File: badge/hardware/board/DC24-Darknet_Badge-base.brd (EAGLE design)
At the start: 48.3 x 83.8 mm, 15 parts, among them U1 SOP22

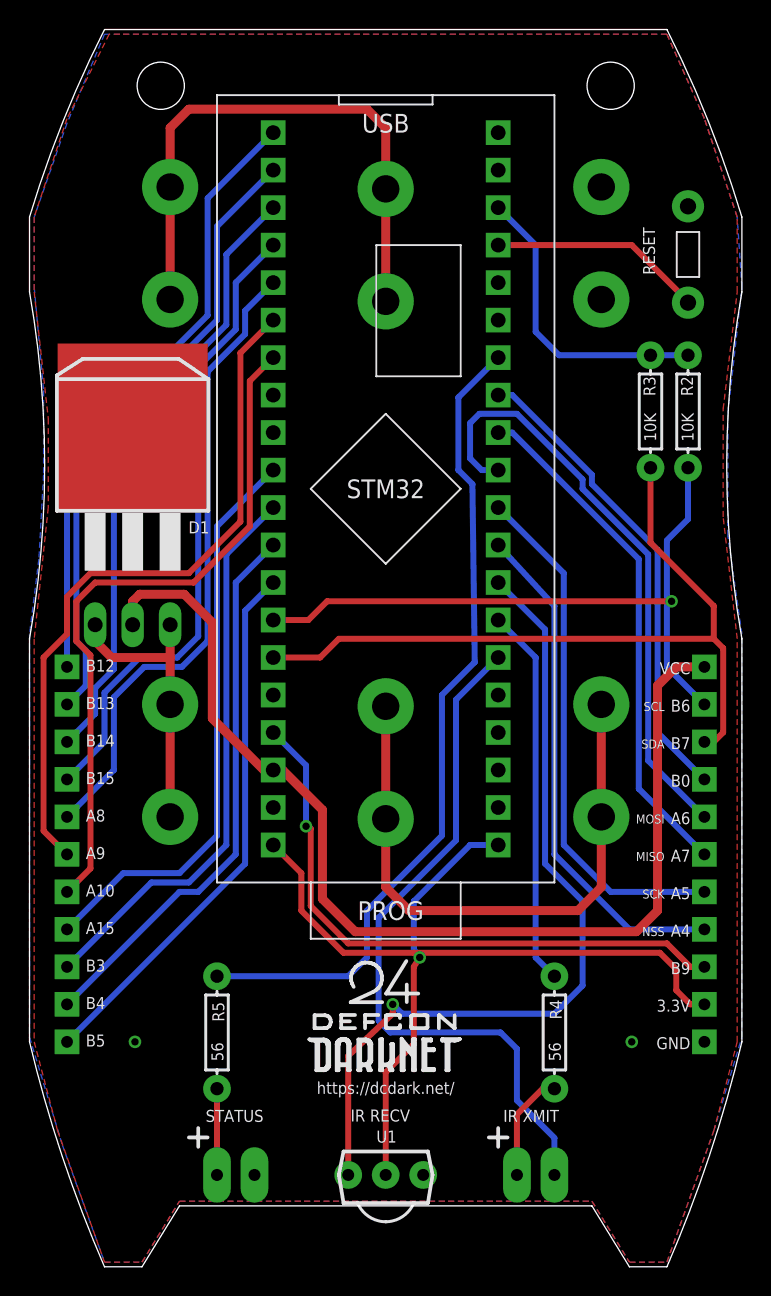
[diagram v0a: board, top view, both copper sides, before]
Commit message: Board design that was made for DEF CON Note there are some problems with ground plane isolation that were not caught which makes this easy to accidentally bridge VCC and GND when soldering.
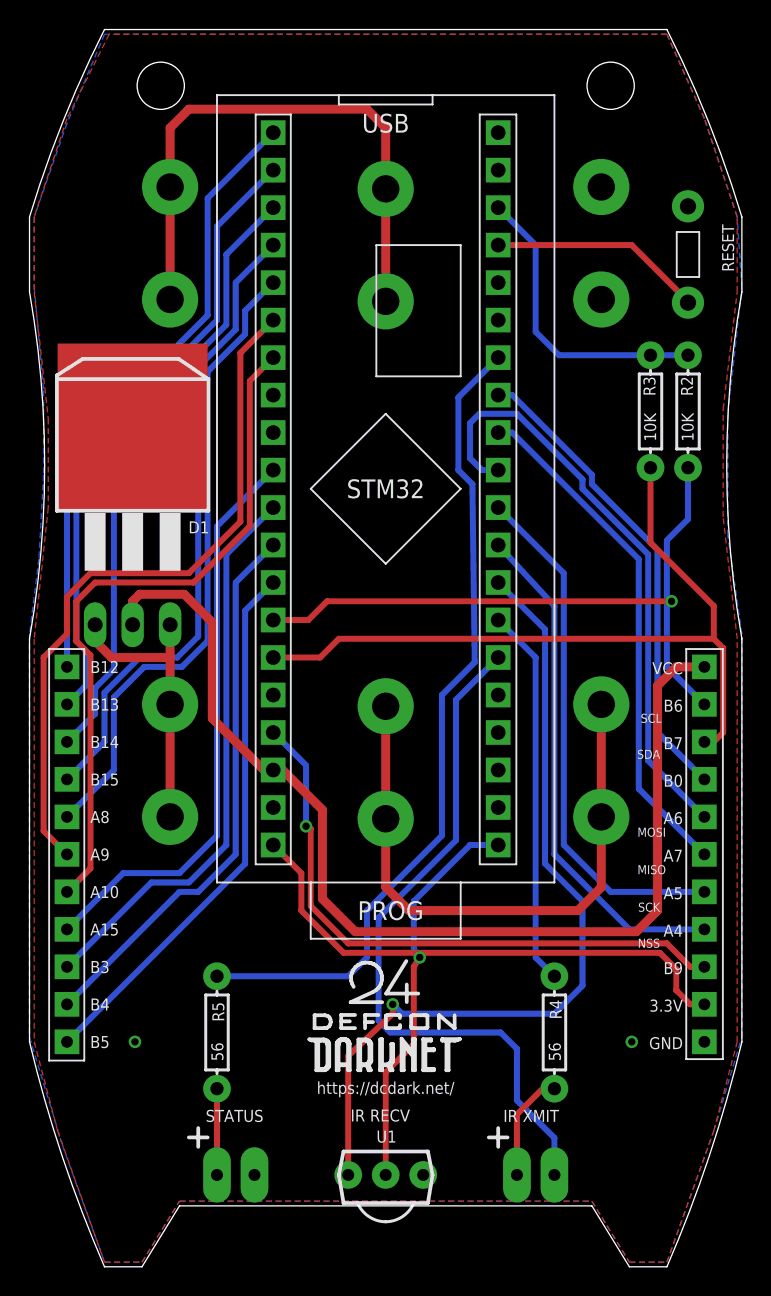
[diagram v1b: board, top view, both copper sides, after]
